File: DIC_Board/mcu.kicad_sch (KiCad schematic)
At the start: 72 parts, among them J1 DM3AT-SF-PEJM5, J2 Conn_ARM_JTAG_SWD_10, P1 USB4105-GF-A, SW1 SW_Push, U1 STM32L476ZGTx, U2 AB-RTCMC-32.768kHz-EOA9-S3, U3 APS6404L-3SQRX-SN, Y1 ABM8AAIG-8.000MHz-V2R-T3, Y2 ABS06-107-32.768KHZ-T

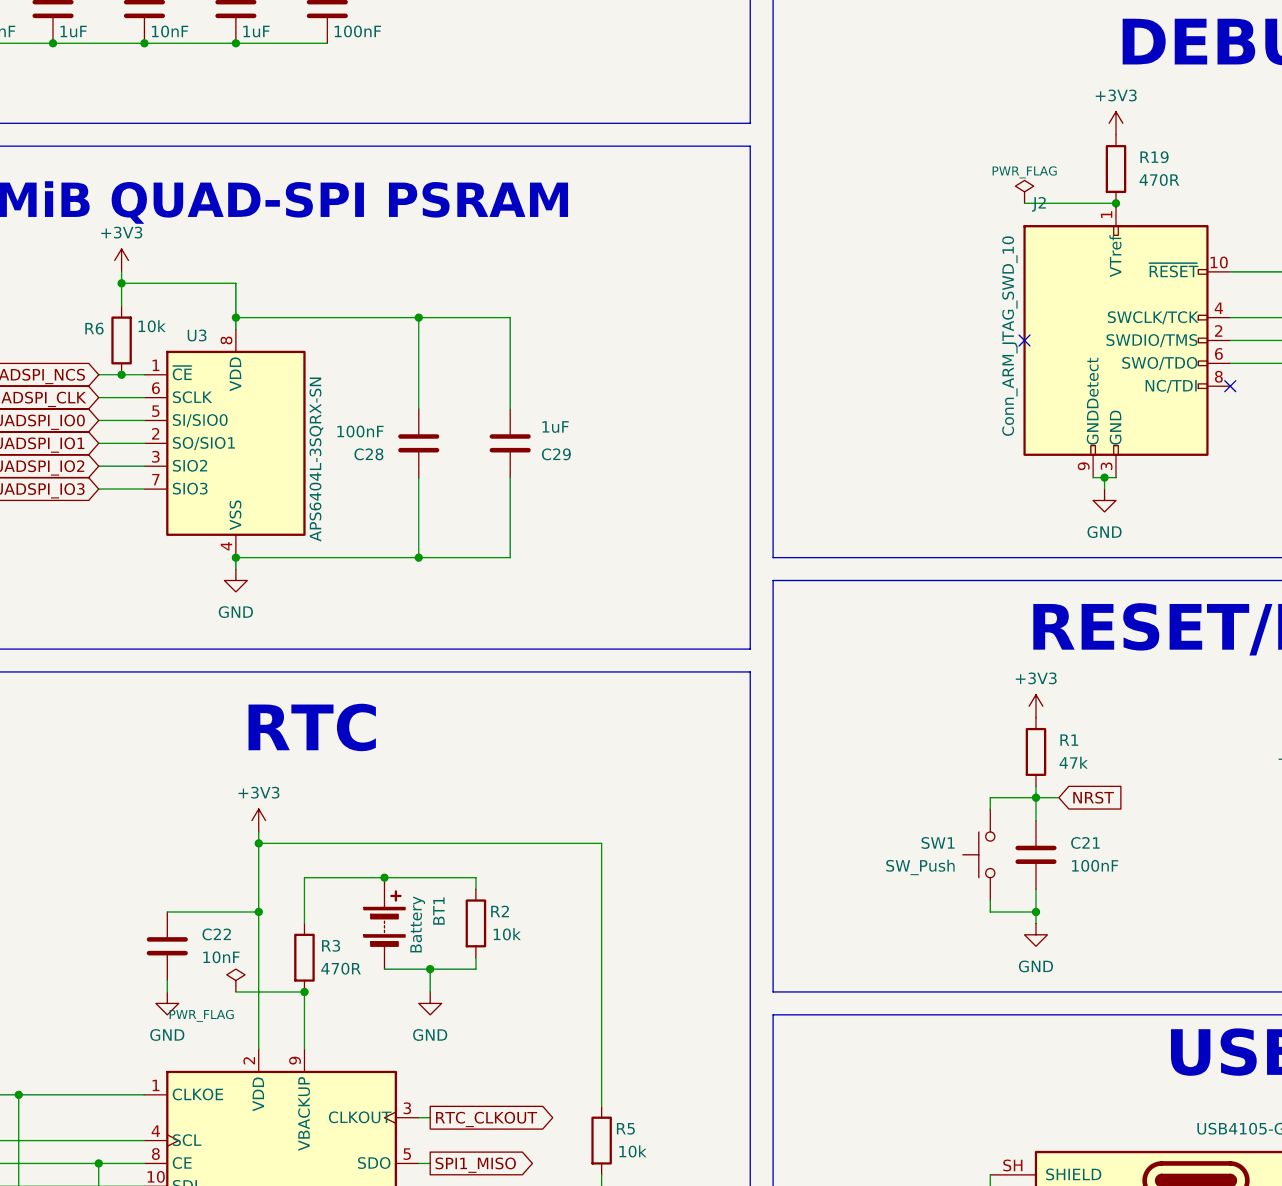
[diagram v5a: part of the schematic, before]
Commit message: resized the board to 9.5 in by 2 in
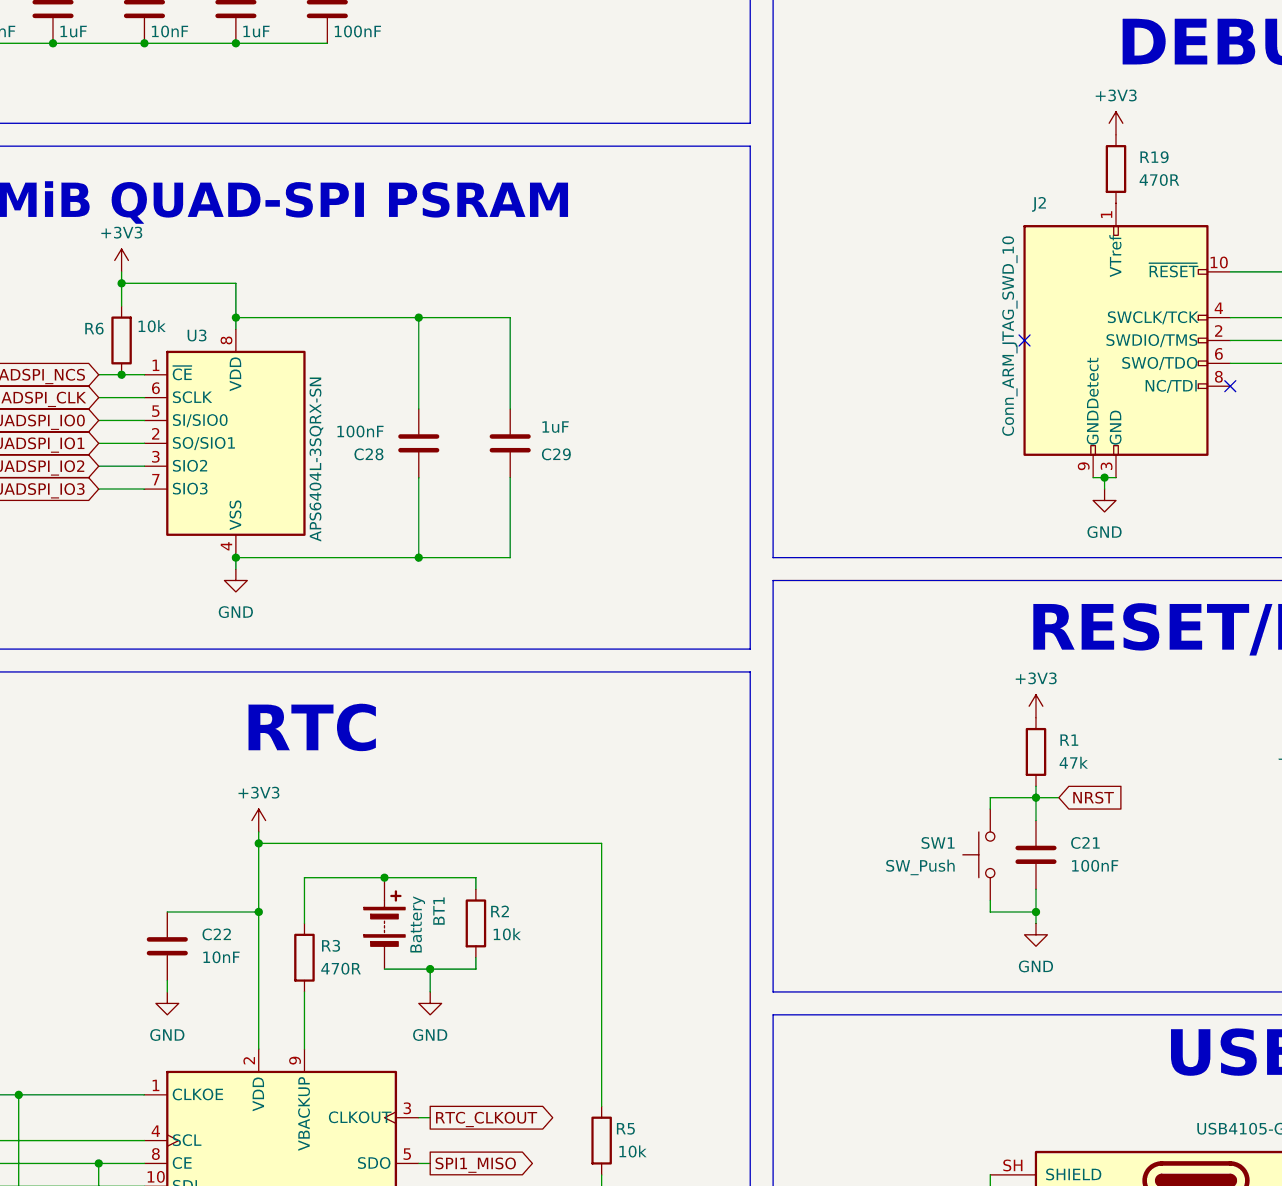
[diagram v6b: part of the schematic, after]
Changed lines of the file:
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@@
 		)
 	)
- (symbol (lib_id "power:PWR_FLAG") (at 57.15 200.66 0) (unit 1)
- (exclude_from_sim no) (in_bom no) (on_board yes) (dnp no)
- (property "Reference" "#FLG0991" (at 57.15 198.755 0) (effects (font (size 1.27 1.27)) (hide yes)))
- (property "Value" "PWR_FLAG" (at 53.34 203.2 0) (effects (font (size 1 1))))
- (property "Footprint" "" (at 57.15 200.66 0) (effects (font (size 1.27 1.27)) (hide yes)))
- (property "Datasheet" "" (at 57.15 200.66 0) (effects (font (size 1.27 1.27)) (hide yes)))
- (pin "1")
- (instances (project "DIC_Board" (path "/bb0ef0df-c181-443a-843c-695cd2e0efee/ef2b3969-ba29-4866-a95a-5e275b2bf226" (reference "#FLG0991") (unit 1)))))
- (wire (pts (xy 57.15 200.66) (xy 64.77 200.66)) (stroke (width 0) (type default)))
- (junction (at 64.77 200.66) (diameter 0) (color 0 0 0 0))
- (symbol (lib_id "power:PWR_FLAG") (at 144.78 113.03 0) (unit 1)
- (exclude_from_sim no) (in_bom no) (on_board yes) (dnp no)
- (property "Reference" "#FLG0992" (at 144.78 111.125 0) (effects (font (size 1.27 1.27)) (hide yes)))
- (property "Value" "PWR_FLAG" (at 144.78 109.474 0) (effects (font (size 1 1))))
- (property "Footprint" "" (at 144.78 113.03 0) (effects (font (size 1.27 1.27)) (hide yes)))
- (property "Datasheet" "" (at 144.78 113.03 0) (effects (font (size 1.27 1.27)) (hide yes)))
- (pin "1")
- (instances (project "DIC_Board" (path "/bb0ef0df-c181-443a-843c-695cd2e0efee/ef2b3969-ba29-4866-a95a-5e275b2bf226" (reference "#FLG0992") (unit 1)))))
- (wire (pts (xy 144.78 113.03) (xy 154.94 113.03)) (stroke (width 0) (type default)))
- (junction (at 154.94 113.03) (diameter 0) (color 0 0 0 0))
 )
